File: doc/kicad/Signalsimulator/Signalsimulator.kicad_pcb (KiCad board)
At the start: 2 copper layers, 38.1 x 38.1 mm, 12 parts, among them J1 Conn_02x03_Odd_Even

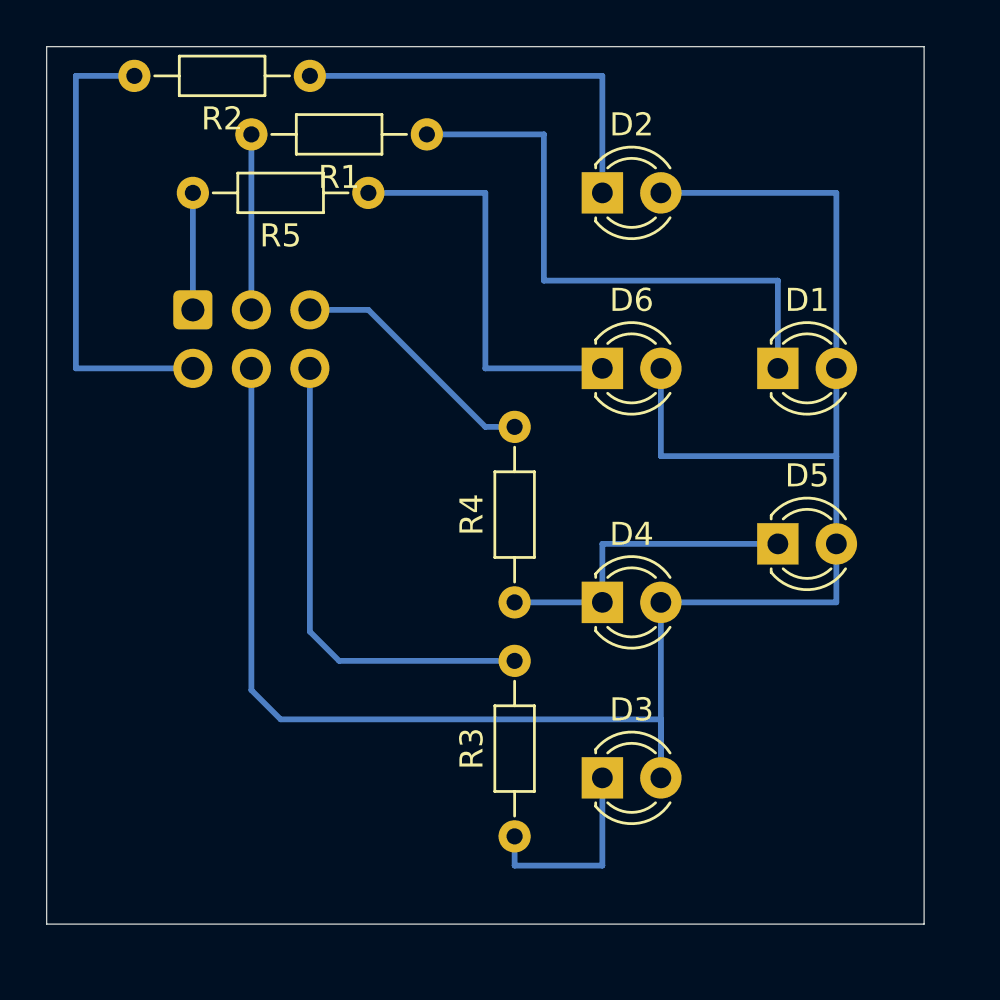
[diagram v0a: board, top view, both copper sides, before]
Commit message: Ecken rund gemacht, alle mit Montagelöcher
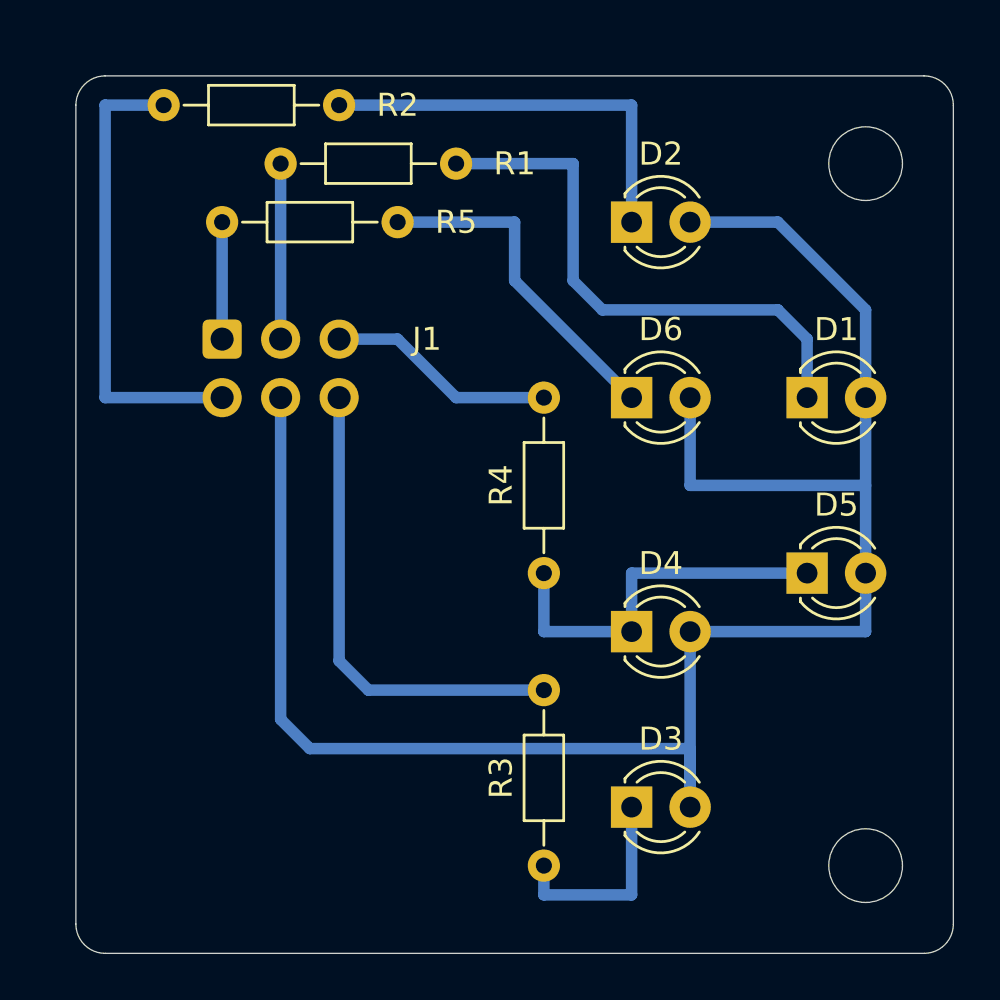
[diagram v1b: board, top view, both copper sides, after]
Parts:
- added H1: MountingHole, Mounting_Holes:MountingHole_3.2mm_M3, F.Cu at (59.7, 29.2)
- added H1: MountingHole, Mounting_Holes:MountingHole_3.2mm_M3, F.Cu at (59.7, 59.7)
- moved D4 1.80 mm to (49.5, 49.5)
- moved D2 1.80 mm to (49.5, 31.8)
- moved D3 1.80 mm to (49.5, 57.1)
- moved D5 1.80 mm to (57.1, 47.0)
- moved D6 1.80 mm to (49.5, 39.4)
- moved R2 1.80 mm to (36.8, 26.7)
- moved J1 1.80 mm to (31.8, 36.8)
- moved R1 1.80 mm to (41.9, 29.2)
- moved R5 1.80 mm to (39.4, 31.8)
- moved D1 1.80 mm to (57.1, 39.4)
- moved R3 1.80 mm to (45.7, 59.7)
- moved R4 1.80 mm to (45.7, 47.0)
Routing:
- net Net-(D6-Pad1): track 17.8 -> 14.8 mm
- net Net-(D4-Pad1): track 14.0 -> 16.5 mm
- net +5P: track 86.9 -> 84.7 mm
- net Net-(D1-Pad1): track 25.4 -> 23.9 mm
- net Net-(J1-Pad5): track 11.0 -> 9.94 mm
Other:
- outline, holes or cut-outs redrawn
- net class Default: trace_width 0.25 -> 0.5
- board text added: "©H3-H5N6 2021 HL-Signal v1.0"

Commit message: Platinen, die an jlcpcb geschickt worden sind.
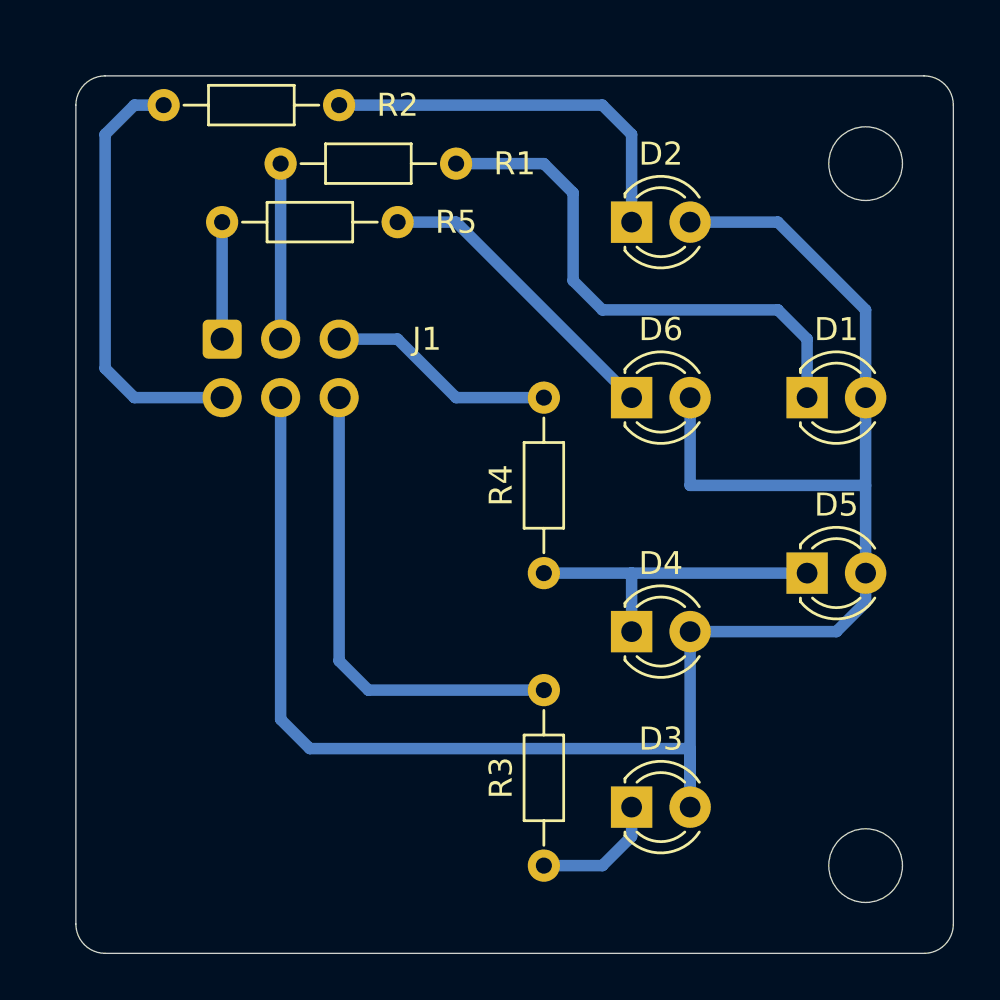
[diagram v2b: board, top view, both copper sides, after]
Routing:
- net Net-(D3-Pad1): track 8.89 -> 5.61 mm
- net Net-(D4-Pad1): track 16.5 -> 14.0 mm
- net Net-(D6-Pad1): track 14.8 -> 13.3 mm
- net Net-(J1-Pad2): track 20.3 -> 18.8 mm
- net +5P: track 84.7 -> 83.9 mm
- net Net-(D2-Pad1): track 17.8 -> 17.0 mm
- net Net-(D1-Pad1): track 23.9 -> 23.2 mm

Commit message: Aufgeräumt
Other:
- net class Default removed

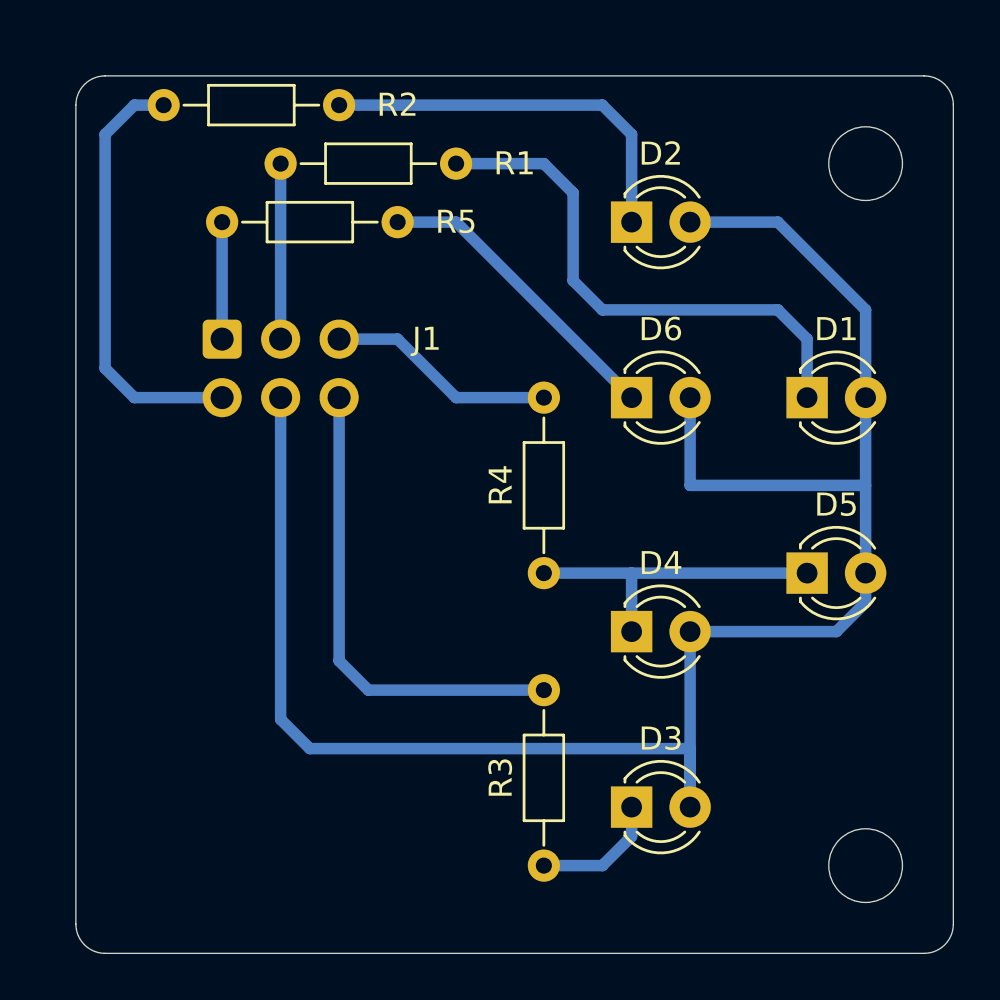
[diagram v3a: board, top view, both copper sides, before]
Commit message: Flächen gefült und DRC-Warnung beseitigt
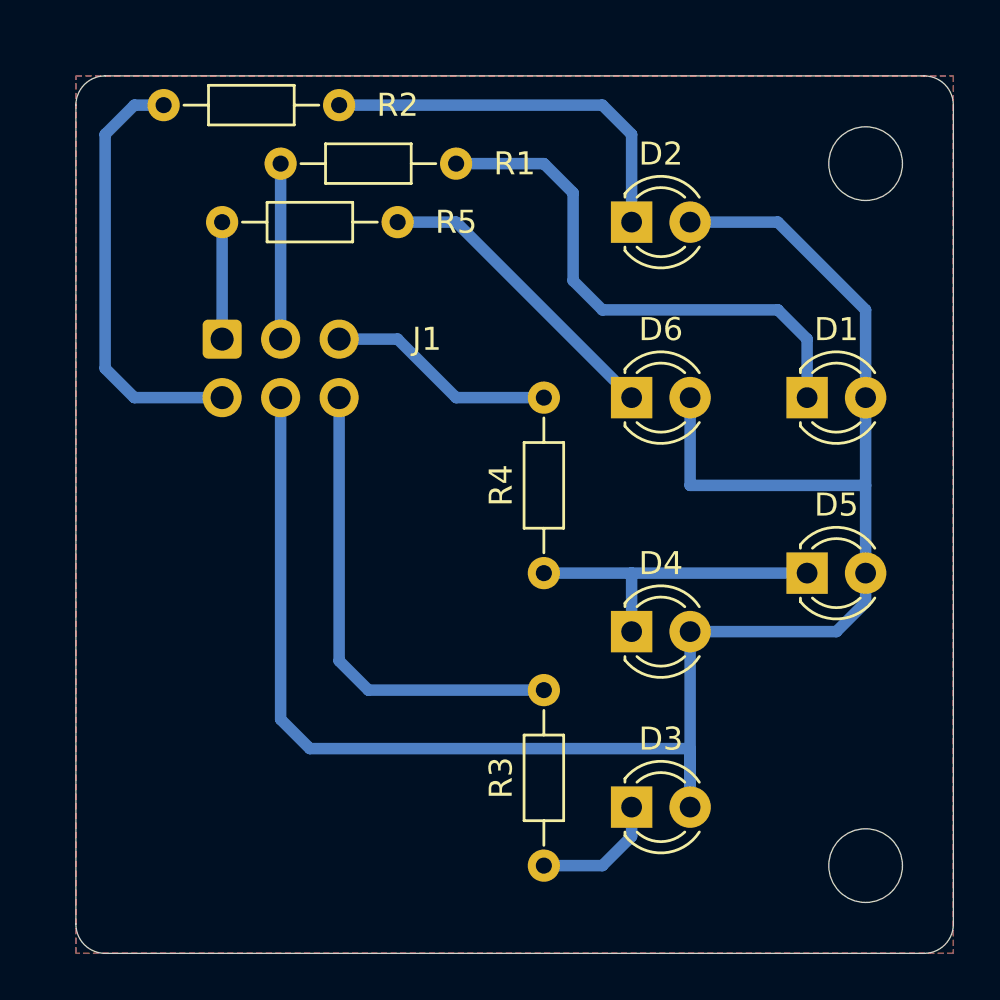
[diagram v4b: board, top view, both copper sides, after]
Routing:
- added copper zone on B.Cu, net (none)
- added copper zone on F.Cu, net (none)
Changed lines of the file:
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@@
   (gr_arc (start 25.4 26.67) (mid 25.771974 25.771974) (end 26.67 25.4) (layer "Edge.Cuts") (width 0.05))
   (gr_arc (start 26.67 63.5) (mid 25.771974 63.128026) (end 25.4 62.23) (layer "Edge.Cuts") (width 0.05))
-  (gr_text "©H3-H5N6 2021\nHL-Signal v1.0" (at 52.07 43.18) (layer "B.SilkS")
+  (gr_text "©H3-H5N6 2021\nHL-Signal v1.0" (at 52.324 43.18) (layer "B.SilkS")
     (effects (font (size 1.5 1.5) (thickness 0.3)) (justify mirror))
   )
@@
   (segment (start 38.1 52.07) (end 45.72 52.07) (width 0.5) (layer "B.Cu") (net 11))
   (segment (start 36.83 39.37) (end 36.83 50.8) (width 0.5) (layer "B.Cu") (net 11))
+  (zone (net 0) (net_name "") (layers F&B.Cu) (hatch edge 0.508)
+    (connect_pads (clearance 0.508))
+    (min_thickness 0.254) (filled_areas_thickness no)
+    (fill yes (thermal_gap 0.508) (thermal_bridge_width 0.508))
+    (polygon
+      (pts
+        (xy 63.5 63.5)
+        (xy 25.4 63.5)
+        (xy 25.4 25.4)
+        (xy 63.5 25.4)
+      )
+    )
+  )
+  (zone (net 0) (net_name "") (layer "F.Cu") (hatch edge 0.508)
+    (connect_pads (clearance 0.508))
+    (min_thickness 0.254) (filled_areas_thickness no)
+    (fill yes (thermal_gap 0.508) (thermal_bridge_width 0.508))
+    (polygon
+      (pts
+        (xy 63.5 63.5)
+        (xy 25.4 63.5)
+        (xy 25.4 25.4)
+        (xy 63.5 25.4)
+      )
+    )
+  )
 )

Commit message: Widerständer auf Rückseite, Widerstandswerte angepasst
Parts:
- R1, R2, R3, R4, R5: moved to B.Cu
- moved R5 1.27 mm to (39.4, 33.0)
- moved R1 1.27 mm to (41.9, 30.5)
- moved R2 1.27 mm to (36.8, 27.9)
- moved R3 1.27 mm to (45.7, 58.4)
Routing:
- net Net-(J1-Pad2): track 18.8 -> 13.2 mm
- net Net-(D1-Pad1): track 23.2 -> 20.4 mm
- net Net-(J1-Pad1): track 5.08 -> 3.81 mm
- net Net-(J1-Pad6): track 20.8 -> 19.6 mm
- net Net-(J1-Pad3): track 7.62 -> 6.35 mm
- net Net-(D2-Pad1): track 17.0 -> 15.8 mm
- net Net-(D3-Pad1): track 5.61 -> 4.34 mm
- net Net-(D6-Pad1): track 13.3 -> 12.8 mm
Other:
- board text added: "HL-Signal v1.1"
- board text added: "©H3-H5N6 2022"
- board text removed: "©H3-H5N6 2021 HL-Signal v1.0"
